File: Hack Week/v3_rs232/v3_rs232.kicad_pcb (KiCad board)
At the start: 2 copper layers, 17.5 x 17 mm, 3 parts, among them J1 DE9_Socket, J2 Conn_01x04_Socket, U1 MAX3232

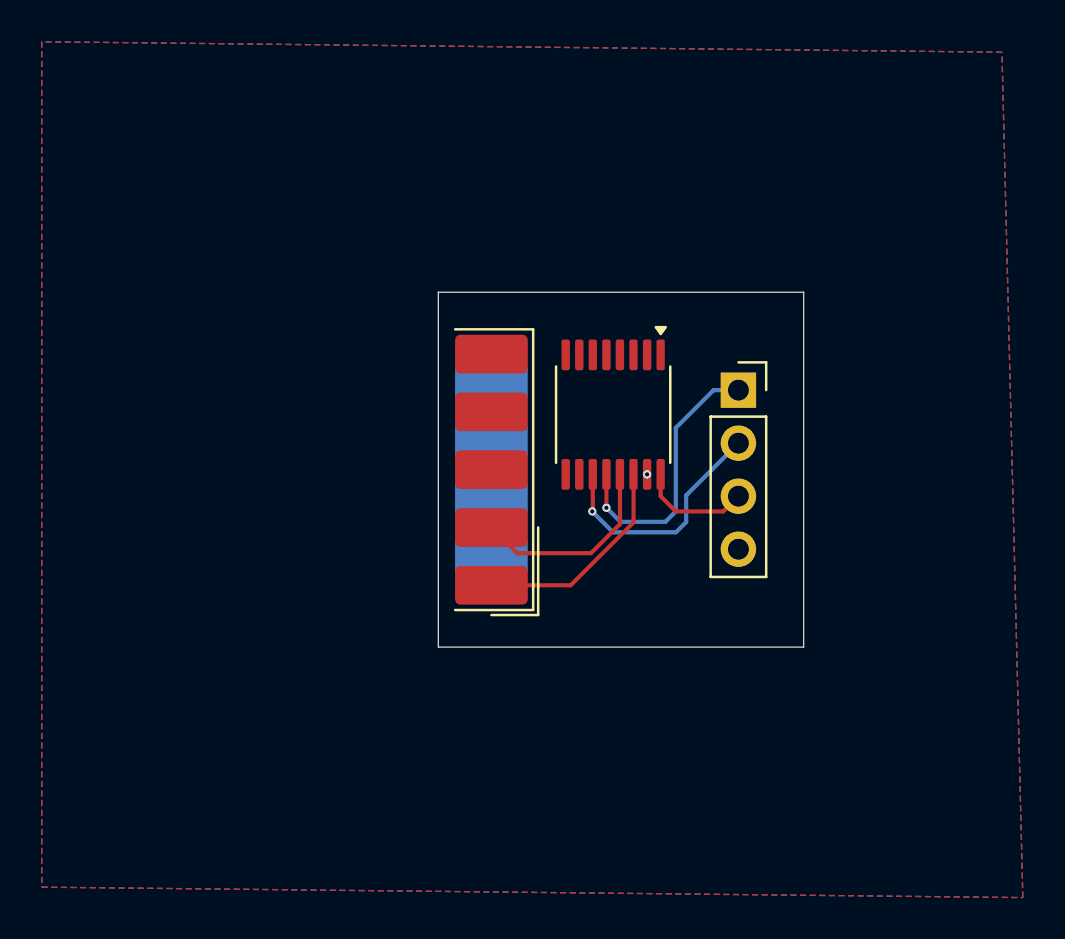
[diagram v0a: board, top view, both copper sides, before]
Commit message: changed DB9 connectors + added RS485
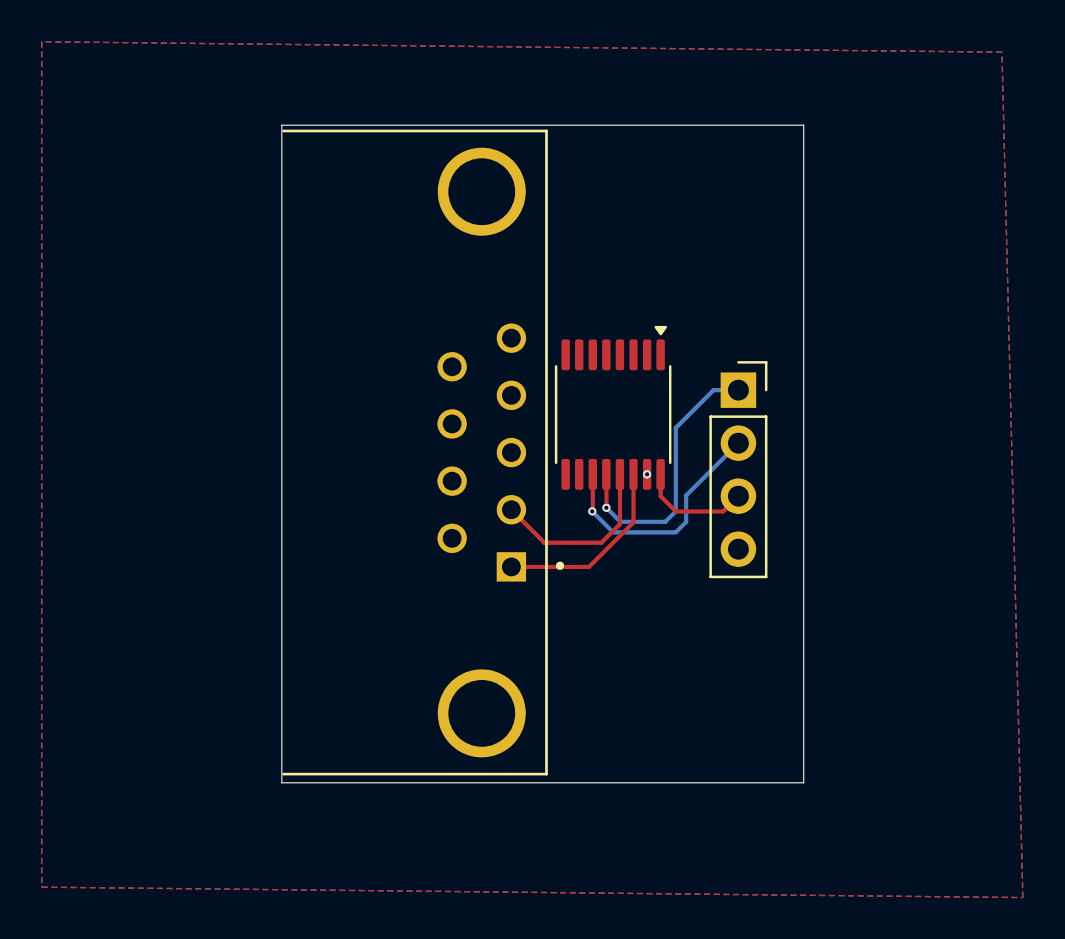
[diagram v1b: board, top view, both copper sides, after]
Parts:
- J1: value DE9_Socket -> LD09S33E4GV00LF; footprint Connector_Dsub:DSUB-9_Socket_EdgeMount_P2.77mm -> Connector_Pin:AMPHENOL_LD09S33E4GV00LF
- moved J1 0.94 mm to (147.1, 93.7)
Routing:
- net Net-(U1-T1OUT): track 10.4 -> 9.03 mm
- net Net-(U1-R1IN): track 9.63 -> 8.61 mm
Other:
- board size 17.5 x 17 mm -> 25 x 31.5 mm
